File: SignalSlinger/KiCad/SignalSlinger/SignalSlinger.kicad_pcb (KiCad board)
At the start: 2 copper layers, 100.3 x 59.1 mm, 100 parts, among them J101 Conn_01x02, J102 Conn_01x02, J103 Conn_01x02, J104 Conn_01x02, J105 Conn_01x02, J106 Conn_01x02, J107 DB9 Female, J108 Conn_01x02, J109 Conn_01x03, J201 Barrel_Jack_Switch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

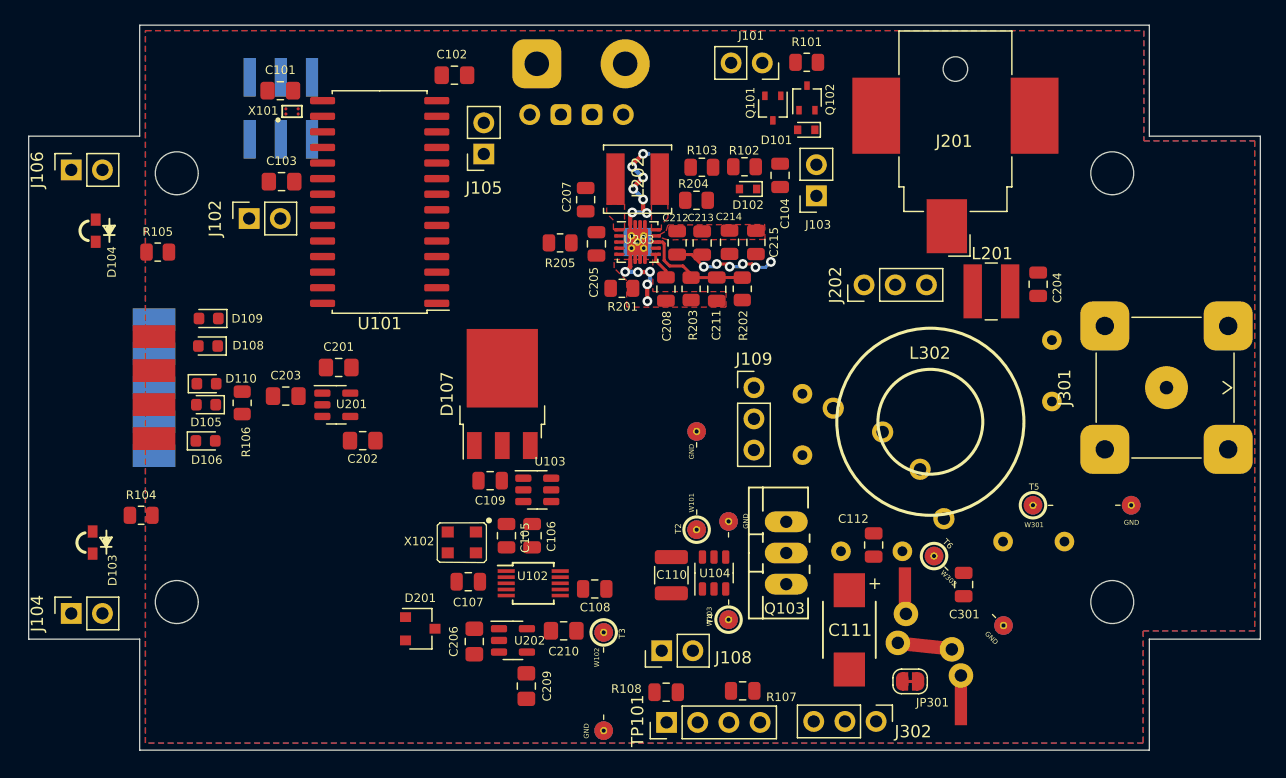
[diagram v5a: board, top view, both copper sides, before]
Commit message: PCB Development
First cut at traces
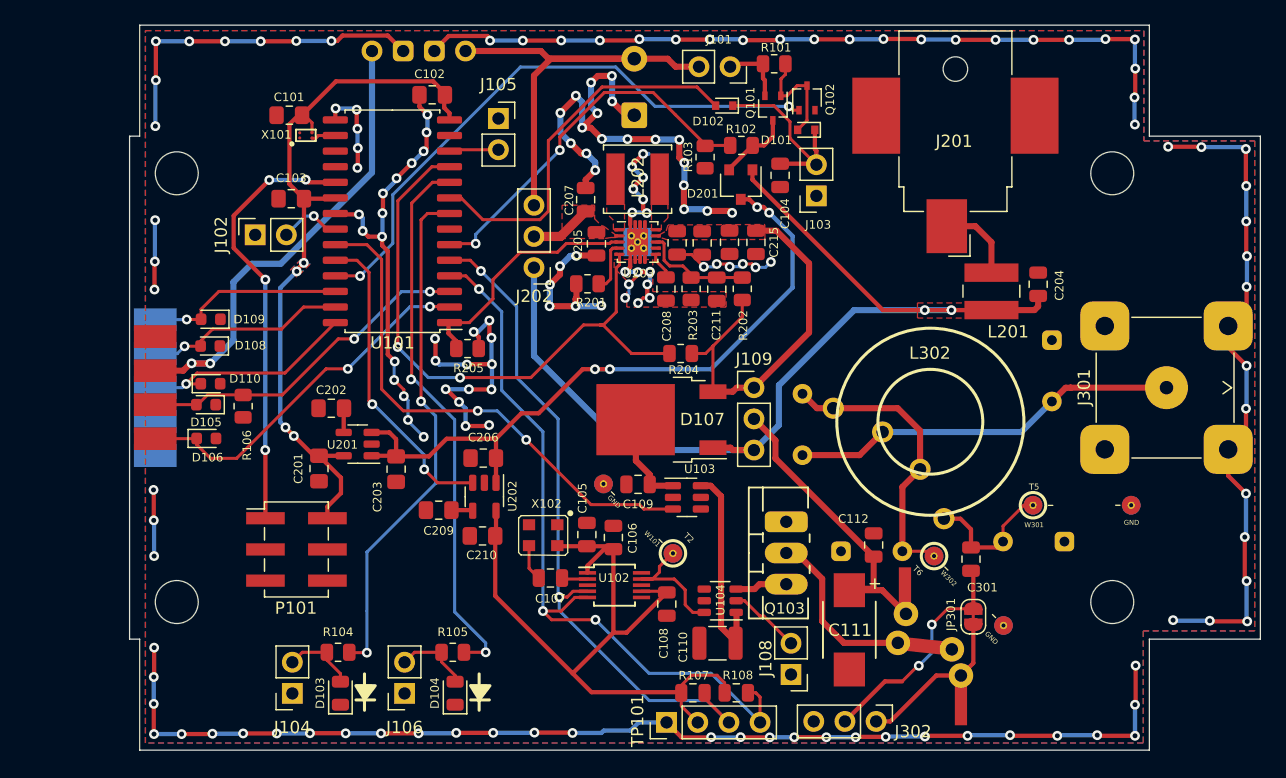
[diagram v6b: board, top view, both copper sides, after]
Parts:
- removed W102: T3, Measurement:Measurement_Point_ScopeProbe_Round-SMD-2sides-Pad_Small
- removed W103: T4, Measurement:Measurement_Point_ScopeProbe_Round-SMD-2sides-Pad_Small
- BT201: footprint Connector_Wire:SolderWire-2.5sqmm_1x02_P7.2mm_D2.4mm_OD3.6mm -> Connector_Wire:SolderWire-0.5sqmm_1x02_P4.6mm_D0.9mm_OD2.1mm
- D103, D104: footprint LED_SMD:LED_APDA1806SECK -> LED_SMD:LED_0805_2012Metric
- D107: footprint Package_TO_SOT_SMD:TO-252-3_TabPin2 -> Package_TO_SOT_SMD:TO-252-2
- P101: moved to F.Cu
- moved J106 50.6 mm to (70.4, 114.3), turned to 180 degrees
- moved D104 47.7 mm to (74.5, 114.3)
- moved D201 44.6 mm to (97.8, 72.9), turned to -90 degrees
- moved R105 40.5 mm to (74.3, 111.0)
- moved P101 36.0 mm to (61.6, 102.6), turned to 0 degrees
- moved J202 26.9 mm to (81.0, 79.6), turned to 180 degrees
- moved D103 23.6 mm to (65.2, 114.3)
- moved R104 19.5 mm to (65.0, 111.0)
- moved J104 19.2 mm to (61.3, 114.3), turned to 180 degrees
- moved C209 16.0 mm to (73.2, 99.4), turned to 180 degrees
- moved C206 15.0 mm to (76.8, 95.2), turned to 0 degrees
- moved MOD201 13.9 mm to (75.4, 62.0)
- moved D107 13.1 mm to (91.3, 92.0), turned to 180 degrees
- moved R204 12.5 mm to (92.9, 86.6), turned to 180 degrees
- moved U103 12.2 mm to (93.4, 98.3)
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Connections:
- BT201 pad 1: +BATT -> GND
- BT201 pad 2: GND -> +BATT
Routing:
- net GND: track 23.5 -> 401.7 mm, vias 18 -> 161
- net V_ext: track 0.00 -> 83.9 mm, vias 0 -> 2
- net VDD: track 0.00 -> 61.0 mm
- net +3V3: track 0.00 -> 60.5 mm, vias 0 -> 4
- net Net-(R108-Pad1): track 0.00 -> 60.0 mm, vias 0 -> 3
- net Net-(C203-Pad2): track 0.00 -> 59.3 mm, vias 0 -> 4
- net Net-(R107-Pad1): track 0.00 -> 56.5 mm, vias 0 -> 2
- net Power_Good: track 0.00 -> 49.8 mm, vias 0 -> 2
- net Power_enable: track 0.00 -> 48.6 mm, vias 0 -> 2
- net Net-(R105-Pad2): track 0.00 -> 44.8 mm, vias 0 -> 2
- net FET_DRIVER_ENABLE: track 0.00 -> 42.6 mm, vias 0 -> 2
- net Net-(R104-Pad2): track 0.00 -> 42.0 mm, vias 0 -> 2
- net V+_Charging: track 0.00 -> 40.2 mm, vias 0 -> 2
- net +BATT: track 0.00 -> 38.8 mm
- net Net-(P101-Pad1): track 0.00 -> 35.3 mm, vias 0 -> 4
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- added copper zone on B.Cu, net +3V3
- added copper zone on F.Cu, net +3V3
- added copper zone on F.Cu, net Net-(C205-Pad2)
- added copper zone on F.Cu, net V_ext
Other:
- board size 100.3 x 59.1 mm -> 92.1 x 59.1 mm
- board text added: "SignalSlinger (TM) Model: SS-80/40 June 2023"

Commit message: PCB Development
Added fan control circuit
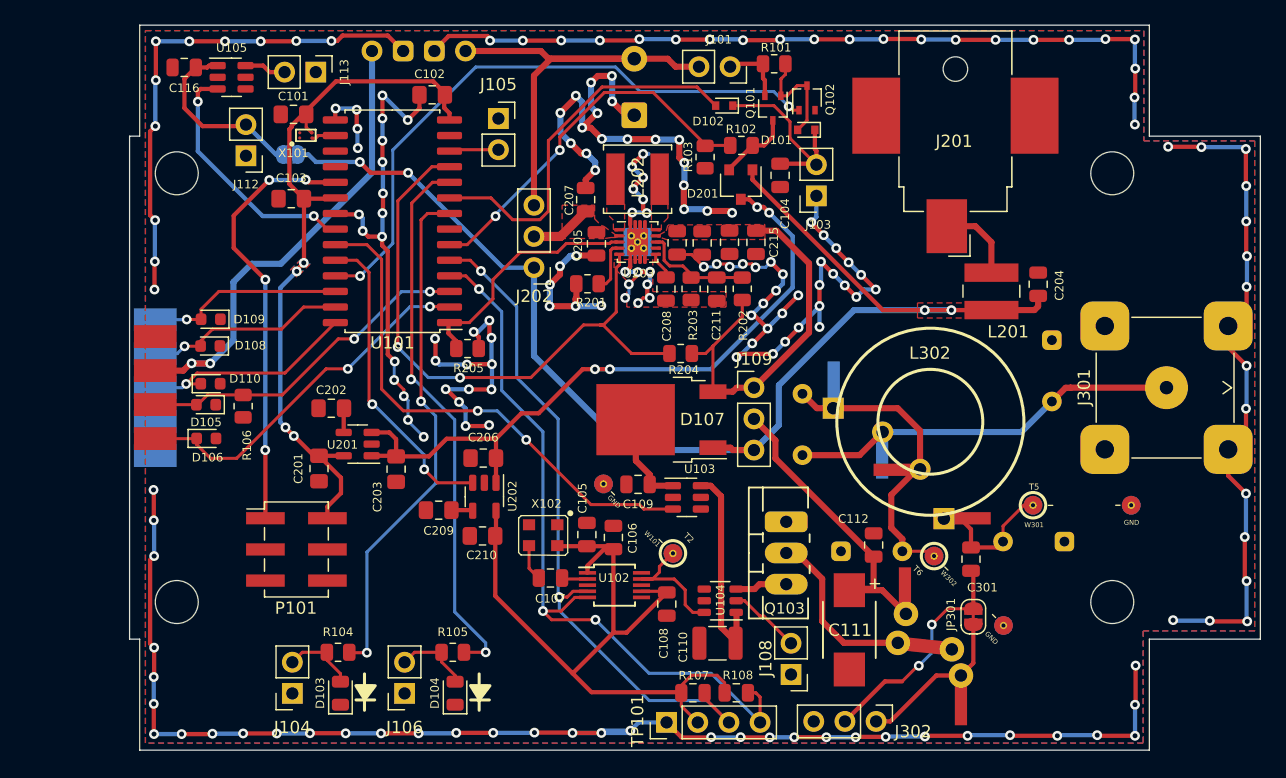
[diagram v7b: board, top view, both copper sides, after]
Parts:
- removed J102: Conn_01x02, Connector_PinSocket_2.54mm:PinSocket_1x02_P2.54mm_Vertical
- added C116: 10uF, Capacitor_SMD:C_0805_2012Metric, F.Cu at (52.5, 63.3)
- added J112: External Power Source, Connector_PinHeader_2.54mm:PinHeader_1x02_P2.54mm_Vertical, F.Cu at (57.5, 70.5)
- added J113: Controlled Power, Connector_PinHeader_2.54mm:PinHeader_1x02_P2.54mm_Vertical, F.Cu at (63.2, 63.7)
- added JP101: V-ext disable, Jumper:SolderJumper-2_P1.3mm_Bridged_RoundedPad1.0x1.5mm, B.Cu at (61.1, 70.4)
- added U105: TPS22810DBVT, Package_TO_SOT_SMD:SOT-23-6, F.Cu at (56.3, 64.1)
- D103: value LED_Filled -> Red LED
- D104: value LED_Filled -> Green LED
- moved C101 0.35 mm to (61.4, 67.2)
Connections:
- U101 pad 22: Net-(J102-Pad2) -> Fan_Contr
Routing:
- net GND: track 401.7 -> 468.8 mm, vias 161 -> 187
- net V_ext: track 83.9 -> 106.9 mm, vias 2 -> 4
- net Fan_Contr: track 0.00 -> 20.4 mm, vias 0 -> 2
- net Net-(J112-Pad2): track 0.00 -> 14.2 mm
- net Net-(J102-Pad2): track 5.06 -> 0.00 mm, vias 1 -> 0
- net Net-(J113-Pad2): track 0.00 -> 3.40 mm
- net Power_enable: track 48.6 -> 50.7 mm
- net Net-(C303-Pad2): track 24.0 -> 24.9 mm
